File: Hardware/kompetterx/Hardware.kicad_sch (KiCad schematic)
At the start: 11 parts

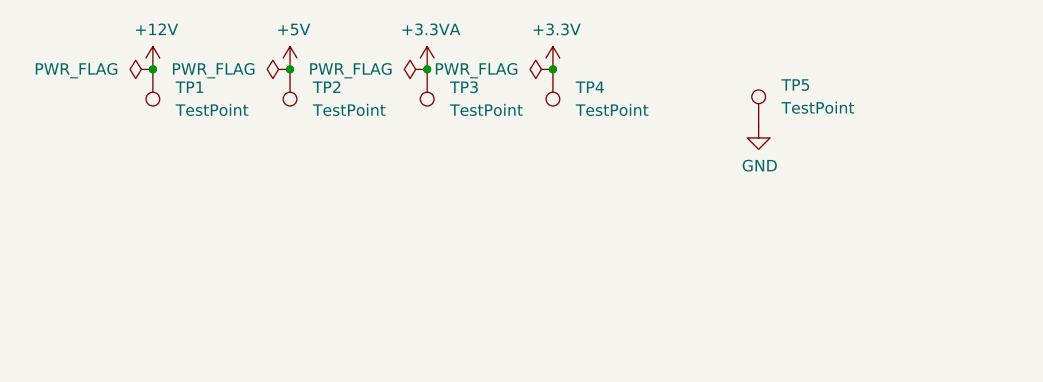
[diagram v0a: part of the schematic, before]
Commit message: Update USB-bug hardware + software
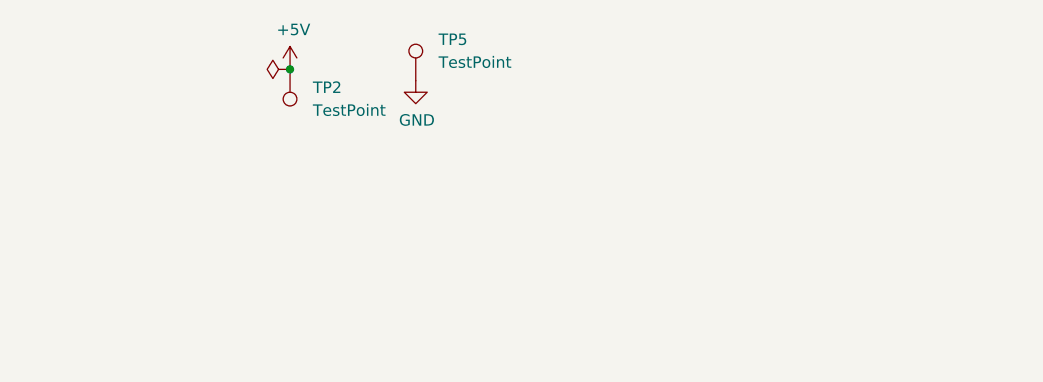
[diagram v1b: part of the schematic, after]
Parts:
- removed TP1, TP3, TP4: TestPoint, TestPoint:TestPoint_Plated_Hole_D2.0mm, symbol Connector:TestPoint
- TP2, TP5: footprint TestPoint:TestPoint_Plated_Hole_D2.0mm -> TestPoint:TestPoint_Pad_D1.0mm
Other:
- moved on the sheet: TP5
